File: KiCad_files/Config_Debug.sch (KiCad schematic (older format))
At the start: 73 parts, among them J12 Conn_01x03, J13 Conn_02x03_Counter_Clockwise, J14 Conn_01x02, J3 Conn_01x06, J4 USB_C_Receptacle, J8 Conn_01x02, J9 Conn_01x02, SW1 SW_Push, U1 XC7A35T_CSG325, U10 W25Q128JV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

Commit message: Finished capacitor footprints
Total cost: ~$55
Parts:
- C219, C220, C224: footprint (none) -> Capacitors_SMD:C_0805
- C221: footprint (none) -> Capacitors_SMD:C_1210
- C222, C223: footprint (none) -> Capacitors_SMD:C_0402
- C69, C70: footprint (none) -> Capacitors_SMD:C_0603
- C71, C72, C73, C74, C75, C76, C77, C78, C79, C80, C81, C82, C83, C84, C85: footprint (none) -> Capacitors_SMD:C_0201
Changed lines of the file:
@@
 F 0 "C82" H 7425 4950 50  0000 L CNN
 F 1 "100uF" H 7425 4750 50  0000 L CNN
-F 2 "" H 7438 4700 50  0001 C CNN
+F 2 "Capacitors_SMD:C_0201" H 7438 4700 50  0001 C CNN
 F 3 "" H 7400 4850 50  0001 C CNN
 	1    7400 4850
@@
 F 0 "C85" H 9975 1100 50  0000 L CNN
 F 1 "0.1uF" H 9975 900 50  0000 L CNN
-F 2 "" H 9988 850 50  0001 C CNN
+F 2 "Capacitors_SMD:C_0201" H 9988 850 50  0001 C CNN
 F 3 "" H 9950 1000 50  0001 C CNN
 	1    9950 1000
@@
 F 0 "C84" H 8225 2050 50  0000 L CNN
 F 1 "0.1uF" H 8225 1850 50  0000 L CNN
-F 2 "" H 8238 1800 50  0001 C CNN
+F 2 "Capacitors_SMD:C_0201" H 8238 1800 50  0001 C CNN
 F 3 "" H 8200 1950 50  0001 C CNN
 	1    8200 1950
@@
 F 0 "C83" H 8175 2900 50  0000 L CNN
 F 1 "0.1uF" H 8175 2700 50  0000 L CNN
-F 2 "" H 8188 2650 50  0001 C CNN
+F 2 "Capacitors_SMD:C_0201" H 8188 2650 50  0001 C CNN
 F 3 "" H 8150 2800 50  0001 C CNN
 	1    8150 2800
@@
 F 0 "C73" H 3110 3470 50  0000 L CNN
 F 1 "27pF" H 3110 3320 50  0000 L CNN
-F 2 "" H 3100 3400 50  0001 C CNN
+F 2 "Capacitors_SMD:C_0201" H 3100 3400 50  0001 C CNN
 F 3 "" H 3100 3400 50  0001 C CNN
 	1    3100 3400
@@
 F 0 "C72" H 3110 3070 50  0000 L CNN
 F 1 "27pF" H 3110 2920 50  0000 L CNN
-F 2 "" H 3100 3000 50  0001 C CNN
+F 2 "Capacitors_SMD:C_0201" H 3100 3000 50  0001 C CNN
 F 3 "" H 3100 3000 50  0001 C CNN
 	1    3100 3000
@@
 F 0 "C69" H 2410 2220 50  0000 L CNN
 F 1 "4.7uF" H 2410 2070 50  0000 L CNN
-F 2 "" H 2400 2150 50  0001 C CNN
+F 2 "Capacitors_SMD:C_0603" H 2400 2150 50  0001 C CNN
 F 3 "" H 2400 2150 50  0001 C CNN
 	1    2400 2150
@@
 F 0 "C71" H 2910 2220 50  0000 L CNN
 F 1 "100nF" H 2910 2070 50  0000 L CNN
-F 2 "" H 2900 2150 50  0001 C CNN
+F 2 "Capacitors_SMD:C_0201" H 2900 2150 50  0001 C CNN
 F 3 "" H 2900 2150 50  0001 C CNN
 	1    2900 2150
@@
 F 0 "C70" H 2660 2220 50  0000 L CNN
 F 1 "4.7uF" H 2660 2070 50  0000 L CNN
-F 2 "" H 2650 2150 50  0001 C CNN
+F 2 "Capacitors_SMD:C_0603" H 2650 2150 50  0001 C CNN
 F 3 "" H 2650 2150 50  0001 C CNN
 	1    2650 2150
@@
 F 0 "C74" H 3160 2220 50  0000 L CNN
 F 1 "100nF" H 3160 2070 50  0000 L CNN
-F 2 "" H 3150 2150 50  0001 C CNN
+F 2 "Capacitors_SMD:C_0201" H 3150 2150 50  0001 C CNN
 F 3 "" H 3150 2150 50  0001 C CNN
 	1    3150 2150
@@
 F 0 "C75" H 5710 2120 50  0000 L CNN
 F 1 "100nF" H 5710 1970 50  0000 L CNN
-F 2 "" H 5700 2050 50  0001 C CNN
+F 2 "Capacitors_SMD:C_0201" H 5700 2050 50  0001 C CNN
 F 3 "" H 5700 2050 50  0001 C CNN
 	1    5700 2050
@@
 F 0 "C77" H 5960 2120 50  0000 L CNN
 F 1 "100nF" H 5960 1970 50  0000 L CNN
-F 2 "" H 5950 2050 50  0001 C CNN
+F 2 "Capacitors_SMD:C_0201" H 5950 2050 50  0001 C CNN
 F 3 "" H 5950 2050 50  0001 C CNN
 	1    5950 2050
@@
 F 0 "C79" H 6210 2120 50  0000 L CNN
 F 1 "100nF" H 6210 1970 50  0000 L CNN
-F 2 "" H 6200 2050 50  0001 C CNN
+F 2 "Capacitors_SMD:C_0201" H 6200 2050 50  0001 C CNN
 F 3 "" H 6200 2050 50  0001 C CNN
 	1    6200 2050
@@
 F 0 "C76" H 5710 2770 50  0000 L CNN
 F 1 "100nF" H 5710 2620 50  0000 L CNN
-F 2 "" H 5700 2700 50  0001 C CNN
+F 2 "Capacitors_SMD:C_0201" H 5700 2700 50  0001 C CNN
 F 3 "" H 5700 2700 50  0001 C CNN
 	1    5700 2700
@@
 F 0 "C78" H 5960 2770 50  0000 L CNN
 F 1 "100nF" H 5960 2620 50  0000 L CNN
-F 2 "" H 5950 2700 50  0001 C CNN
+F 2 "Capacitors_SMD:C_0201" H 5950 2700 50  0001 C CNN
 F 3 "" H 5950 2700 50  0001 C CNN
 	1    5950 2700
@@
 F 0 "C80" H 6210 2770 50  0000 L CNN
 F 1 "100nF" H 6210 2620 50  0000 L CNN
-F 2 "" H 6200 2700 50  0001 C CNN
+F 2 "Capacitors_SMD:C_0201" H 6200 2700 50  0001 C CNN
 F 3 "" H 6200 2700 50  0001 C CNN
 	1    6200 2700
@@
 F 0 "C81" H 6460 2770 50  0000 L CNN
 F 1 "100nF" H 6460 2620 50  0000 L CNN
-F 2 "" H 6450 2700 50  0001 C CNN
+F 2 "Capacitors_SMD:C_0201" H 6450 2700 50  0001 C CNN
 F 3 "" H 6450 2700 50  0001 C CNN
 	1    6450 2700
@@
 F 0 "C221" H 7725 4950 50  0000 L CNN
 F 1 "100uF" H 7725 4750 50  0000 L CNN
-F 2 "" H 7738 4700 50  0001 C CNN
+F 2 "Capacitors_SMD:C_1210" H 7738 4700 50  0001 C CNN
 F 3 "" H 7700 4850 50  0001 C CNN
 	1    7700 4850
@@
 F 0 "C224" H 10225 1100 50  0000 L CNN
 F 1 "10uF" H 10225 900 50  0000 L CNN
-F 2 "" H 10238 850 50  0001 C CNN
+F 2 "Capacitors_SMD:C_0805" H 10238 850 50  0001 C CNN
 F 3 "" H 10200 1000 50  0001 C CNN
 	1    10200 1000
@@
 F 0 "C222" H 7925 2900 50  0000 L CNN
 F 1 "1uF" H 7925 2700 50  0000 L CNN
-F 2 "" H 7938 2650 50  0001 C CNN
+F 2 "Capacitors_SMD:C_0402" H 7938 2650 50  0001 C CNN
 F 3 "" H 7900 2800 50  0001 C CNN
 	1    7900 2800
@@
 F 0 "C223" H 7975 2050 50  0000 L CNN
 F 1 "1uF" H 7975 1850 50  0000 L CNN
-F 2 "" H 7988 1800 50  0001 C CNN
+F 2 "Capacitors_SMD:C_0402" H 7988 1800 50  0001 C CNN
 F 3 "" H 7950 1950 50  0001 C CNN
 	1    7950 1950
@@
 F 0 "C220" H 3175 1550 50  0000 L CNN
 F 1 "10uF" H 3175 1350 50  0000 L CNN
-F 2 "" H 3188 1300 50  0001 C CNN
+F 2 "Capacitors_SMD:C_0805" H 3188 1300 50  0001 C CNN
 F 3 "" H 3150 1450 50  0001 C CNN
 	1    3150 1450
@@
 F 0 "C219" H 2925 1550 50  0000 L CNN
 F 1 "10uF" H 2925 1350 50  0000 L CNN
-F 2 "" H 2938 1300 50  0001 C CNN
+F 2 "Capacitors_SMD:C_0805" H 2938 1300 50  0001 C CNN
 F 3 "" H 2900 1450 50  0001 C CNN
 	1    2900 1450

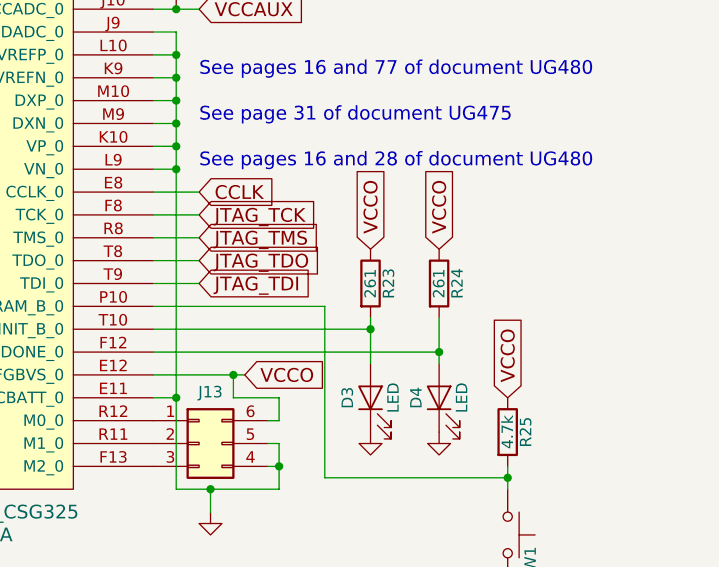
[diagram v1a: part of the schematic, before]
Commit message: Almost done with footprints. See issues below
Inductors left to do.
Others without footprints need custom.
PI3420 is out of stock...
LM2676 symbol should be re-drawn for TO-263-7
Total cost: ~$214
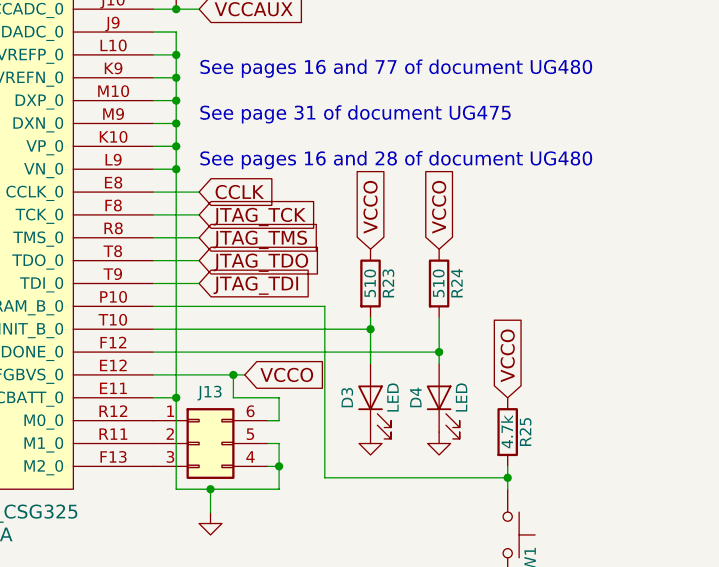
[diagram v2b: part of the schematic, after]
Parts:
- D3, D4, D5, D6, D7: footprint (none) -> LEDs:LED_0603
- J12: footprint (none) -> Pin_Headers:Pin_Header_Straight_1x03_Pitch2.54mm
- J13: footprint (none) -> Pin_Headers:Pin_Header_Straight_2x03_Pitch2.54mm_SMD
- J14, J8, J9: footprint (none) -> Pin_Headers:Pin_Header_Straight_1x02_Pitch2.54mm
- J3: footprint (none) -> Pin_Headers:Pin_Header_Straight_2x03_Pitch2.54mm
- J4: footprint (none) -> Connectors_USB:USB_C_Receptacle_Amphenol_12401610E4-2A
- R10, R11, R12, R13, R14, R15, R16, R17, R18, R19, R20, R21, R22, R25, R28, R31, R7, R76, R8, R9: footprint (none) -> Resistors_SMD:R_0402
- R23, R24: value 261 -> 510; footprint (none) -> Resistors_SMD:R_0402
- SW1: footprint (none) -> Buttons_Switches_SMD:SW_SPST_PTS645
- TP18, TP19, TP20, TP21, TP22, TP23: footprint (none) -> Measurement_Points:Measurement_Point_Round-SMD-Pad_Small
- U10, U7: footprint (none) -> SMD_Packages:SOIC-8-N
- Y1: footprint (none) -> Crystals:Crystal_SMD_HC49-SD

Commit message: Drew some more footprints
BTW another DRC error popped up since I2C level shifter now uses VCC5V0
TODO:
FPGA footprint + Inductors and FETs
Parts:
- U6: footprint (none) -> Housings_QFP:LQFP-64_10x10mm_Pitch0.5mm
- U8: footprint (none) -> custom:4-SMD
- U9: footprint (none) -> custom:6-SMD
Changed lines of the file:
@@
 F 0 "U8" H 8900 2350 60  0000 C CNN
 F 1 "SiT8209" H 8900 1900 60  0000 C CNN
-F 2 "" H 8850 2100 60  0001 C CNN
+F 2 "custom:4-SMD" H 8850 2100 60  0001 C CNN
 F 3 "" H 8850 2100 60  0001 C CNN
 	1    8900 2100
@@
 F 0 "U9" H 8900 3150 60  0000 C CNN
 F 1 "SiT9102" H 8900 2650 60  0000 C CNN
-F 2 "" H 8850 2900 60  0001 C CNN
+F 2 "custom:6-SMD" H 8850 2900 60  0001 C CNN
 F 3 "" H 8850 2900 60  0001 C CNN
 	1    8900 2900
@@
 F 0 "U6" H 4150 1600 50  0000 C CNN
 F 1 "FT2232HL" H 4150 1500 50  0000 C CNN
-F 2 "" H 4150 2100 50  0001 C CNN
+F 2 "Housings_QFP:LQFP-64_10x10mm_Pitch0.5mm" H 4150 2100 50  0001 C CNN
 F 3 "http://www.ftdichip.com/Support/Documents/DataSheets/ICs/DS_FT2232H.pdf" H 4150 2000 50  0001 C CNN
 F 4 "FT2232HL" H 4150 1700 50  0001 C CNN "MPN"

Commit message: Inductors and FETs footprints
TODO:
FPGA and HDMI foorprints
Layout
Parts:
- L4, L5: footprint (none) -> Inductors_SMD:L_0805
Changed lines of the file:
@@
 F 0 "L4" V 2100 1800 50  0000 C CNN
 F 1 "L_Core_Iron" V 2260 1800 50  0000 C CNN
-F 2 "" H 2150 1800 50  0001 C CNN
+F 2 "Inductors_SMD:L_0805" H 2150 1800 50  0001 C CNN
 F 3 "" H 2150 1800 50  0001 C CNN
 	1    2150 1800
@@
 F 0 "L5" V 2100 2000 50  0000 C CNN
 F 1 "L_Core_Iron" V 2260 2000 50  0000 C CNN
-F 2 "" H 2150 2000 50  0001 C CNN
+F 2 "Inductors_SMD:L_0805" H 2150 2000 50  0001 C CNN
 F 3 "" H 2150 2000 50  0001 C CNN
 	1    2150 2000

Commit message: Drew FPGA and HDMI footprints
Ready for layout...?
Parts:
- U1: footprint (none) -> custom:BGA-324_15.0x15.0mm_Layout18x18_P0.8mm_Ball0.5mm_Pad0.4mm_NSMD
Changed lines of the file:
@@
 F 0 "U1" H 8300 5300 60  0000 C CNN
 F 1 "XC7A35T_CSG325" H 8300 5400 60  0000 C CNN
-F 2 "" H 8600 7350 60  0001 C CNN
+F 2 "custom:BGA-324_15.0x15.0mm_Layout18x18_P0.8mm_Ball0.5mm_Pad0.4mm_NSMD" H 8600 7350 60  0001 C CNN
 F 3 "" H 8600 7350 60  0001 C CNN
 	1    8300 5600
